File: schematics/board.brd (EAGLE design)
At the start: 49.2 x 38.1 mm, 25 parts, among them IC1 MEGA8-P, M1 PSMN017-30ELL-V, M2 PSMN017-30ELL-V, M3 PSMN017-30ELL-V

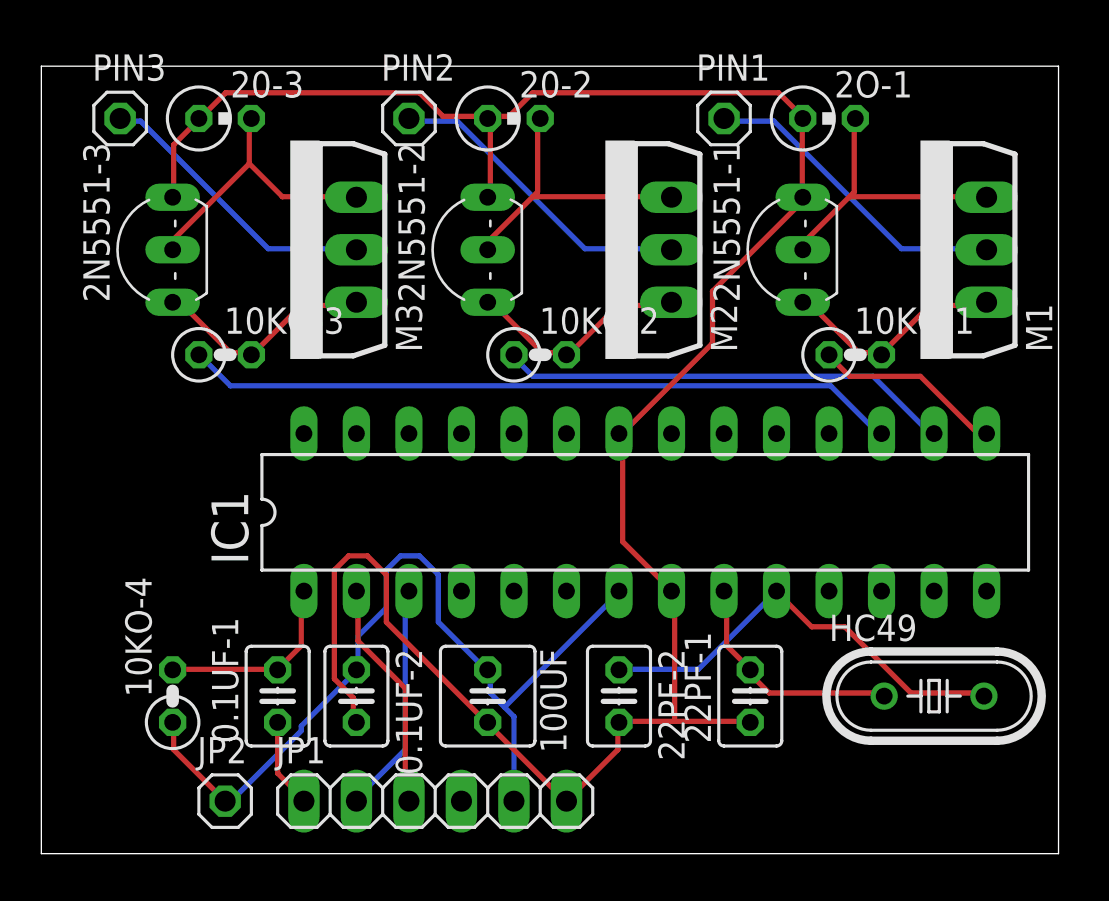
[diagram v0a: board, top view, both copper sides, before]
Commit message: Ajoute alim & logo sur la PCB
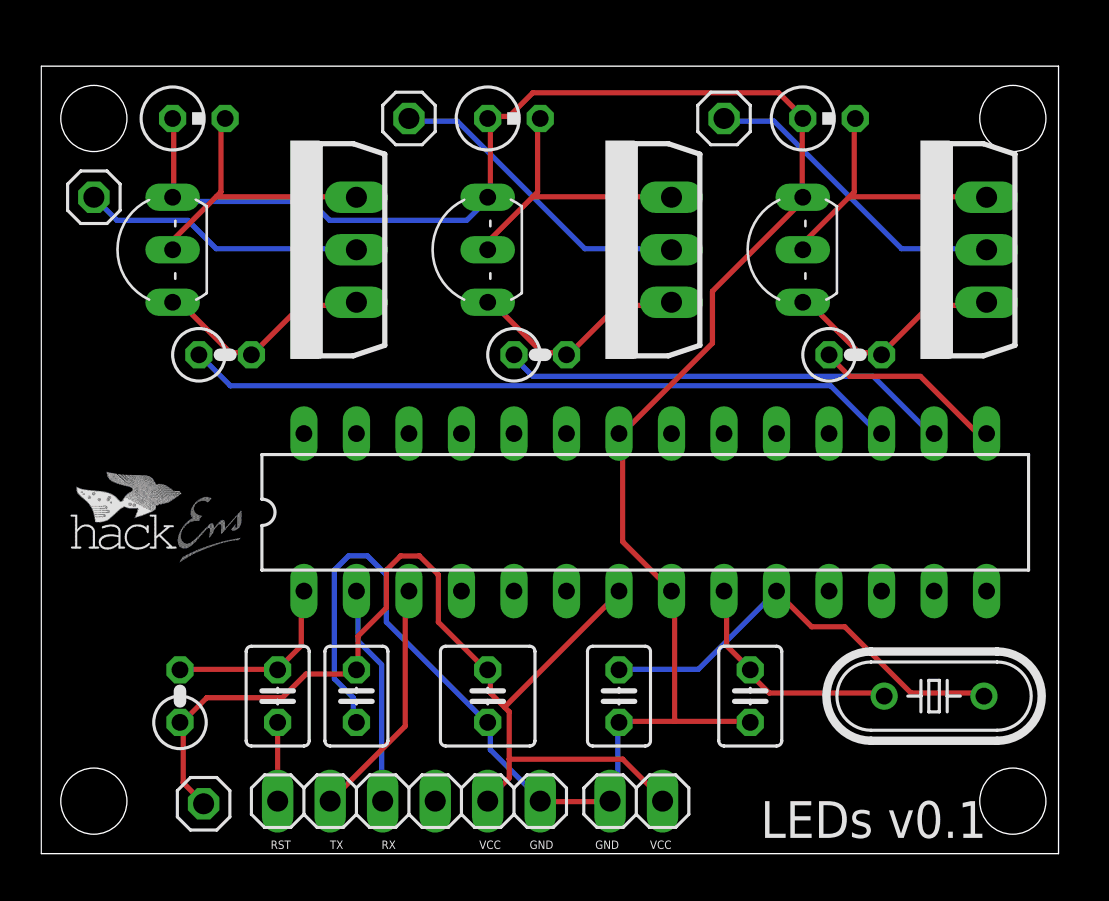
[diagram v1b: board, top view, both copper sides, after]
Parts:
- added POWER: (no value), pinhead:1X02
- added U$1: (no value), hackens:HACKENS-LOGO
- 0.1UF-1, 0.1UF-2: value 0.1μF -> 0.1uF
- 100UF: value 100μF -> 100uF
- 10KO-1, 10KO-2, 10KO-3, 10KO-4: value 10kΩ -> 10k
- 20-2, 20-3, 2O-1: value 2Ω -> 2, 0.6W
- M1, M2, M3: value PSMN017-30ELL-V -> PSMN017-30EL
- moved PIN3 4.02 mm to (2.54, 31.8)
- moved 20-3 1.27 mm to (7.62, 35.6)
- moved JP1 1.27 mm to (17.8, 2.54)
- moved JP2 1.05 mm to (7.85, 2.41)
- moved 10KO-4 0.36 mm to (6.71, 7.62)
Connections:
- net GND: now also POWER.2
- net VCC: now also POWER.1
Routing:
- net VCC: track 43.1 -> 51.6 mm
- net GND: track 110.5 -> 113.2 mm
- net N$9: track 11.2 -> 11.8 mm
- net N$12: track 11.2 -> 10.7 mm
- net N$3: track 4.32 -> 3.81 mm
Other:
- board text added: "GND"
- board text added: "LEDs v0.1"
- board text added: "RST"
- board text added: "RX"
- board text added: "TX"
- board text added: "VCC"

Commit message: Bigger logo
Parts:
- moved U$1 7.73 mm to (0.00, 21.6), turned to 270 degrees
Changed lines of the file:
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@@
 <attribute name="VALUE" x="31.3182" y="5.715" size="1.27" layer="27" rot="R180"/>
 </element>
-<element name="U$1" library="hackens" package="HACKENS-LOGO" value="" x="1.27" y="13.97"/>
+<element name="U$1" library="hackens" package="HACKENS-LOGO" value="" x="0" y="21.59" rot="R270"/>
 </elements>
 <signals>

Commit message: Ajout pins upload
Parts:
- added JP3: (no value), pinhead:1X02
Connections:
- new net N$19: IC1.28, JP3.1
- net GND: now also JP3.2
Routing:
- net GND: track 113.2 -> 121.3 mm
- net N$19: track 0.00 -> 6.69 mm
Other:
- board text added: "upload"
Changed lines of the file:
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@@
 <hole x="2.54" y="2.54" drill="3.2"/>
 <hole x="2.54" y="35.56" drill="3.2"/>
+<text x="5.08" y="11.43" size="1.016" layer="21">upload</text>
 </plain>
 <attributes>
@@
 </element>
 <element name="U$1" library="hackens" package="HACKENS-LOGO" value="" x="0" y="21.59" rot="R270"/>
+<element name="JP3" library="pinhead" package="1X02" value="" x="7.62" y="15.24" smashed="yes" rot="R270">
+<attribute name="VALUE" x="4.445" y="17.78" size="1.27" layer="27" rot="R270"/>
+</element>
 </elements>
 <signals>
@@
 <contactref element="22PF-1" pad="1"/>
 <contactref element="POWER" pad="2"/>
+<contactref element="JP3" pad="2"/>
 <wire x1="6.4008" y1="35.433" x2="6.4008" y2="31.7754" width="0.254" layer="1"/>
 <wire x1="6.4008" y1="31.7754" x2="6.35" y2="31.75" width="0.254" layer="1"/>
@@
 <wire x1="6.4008" y1="31.5468" x2="6.35" y2="31.75" width="0.254" layer="16"/>
 <wire x1="21.4884" y1="31.5468" x2="21.59" y2="31.75" width="0.254" layer="16"/>
-<wire x1="15.0876" y1="7.5438" x2="15.0876" y2="6.4008" width="0.254" layer="16"/>
-<wire x1="14.1732" y1="8.4582" x2="15.0876" y2="7.5438" width="0.254" layer="16"/>
-<wire x1="14.1732" y1="13.716" x2="14.1732" y2="8.4582" width="0.254" layer="16"/>
-<wire x1="14.859" y1="14.4018" x2="14.1732" y2="13.716" width="0.254" layer="16"/>
-<wire x1="15.7734" y1="14.4018" x2="14.859" y2="14.4018" width="0.254" layer="16"/>
-<wire x1="16.6878" y1="13.4874" x2="15.7734" y2="14.4018" width="0.254" layer="16"/>
-<wire x1="16.6878" y1="11.2014" x2="16.6878" y2="13.4874" width="0.254" layer="16"/>
-<wire x1="21.4884" y1="6.4008" x2="16.6878" y2="11.2014" width="0.254" layer="16"/>
+<wire x1="15.0876" y1="6.858" x2="15.0876" y2="6.4008" width="0.254" layer="16"/>
+<wire x1="7.7724" y1="14.1732" x2="12.1158" y2="9.8298" width="0.254" layer="16"/>
+<wire x1="12.1158" y1="9.8298" x2="15.0876" y2="6.858" width="0.254" layer="16"/>
 <wire x1="15.0876" y1="6.4008" x2="15.24" y2="6.35" width="0.254" layer="16"/>
-<wire x1="21.4884" y1="6.4008" x2="21.59" y2="6.35" width="0.254" layer="16"/>
+<wire x1="7.7724" y1="14.1732" x2="7.62" y2="13.97" width="0.254" layer="16"/>
+<wire x1="21.717" y1="5.0292" x2="21.717" y2="6.1722" width="0.254" layer="16"/>
+<wire x1="24.003" y1="2.7432" x2="21.717" y2="5.0292" width="0.254" layer="16"/>
+<wire x1="21.717" y1="6.1722" x2="21.59" y2="6.35" width="0.254" layer="16"/>
+<wire x1="24.003" y1="2.7432" x2="24.13" y2="2.54" width="0.254" layer="16"/>
 <wire x1="36.8046" y1="35.433" x2="36.8046" y2="31.7754" width="0.254" layer="1"/>
 <wire x1="36.8046" y1="31.7754" x2="36.83" y2="31.75" width="0.254" layer="1"/>
@@
 <wire x1="28.1178" y1="20.1168" x2="27.94" y2="20.32" width="0.254" layer="1"/>
 <wire x1="30.4038" y1="12.8016" x2="30.48" y2="12.7" width="0.254" layer="1"/>
-<wire x1="27.432" y1="2.5146" x2="24.2316" y2="2.5146" width="0.254" layer="1"/>
-<wire x1="24.2316" y1="2.5146" x2="24.13" y2="2.54" width="0.254" layer="1"/>
-<wire x1="27.432" y1="2.5146" x2="27.5082" y2="2.54" width="0.254" layer="1"/>
 <wire x1="32.4612" y1="27.2034" x2="36.8046" y2="31.5468" width="0.254" layer="1"/>
 <wire x1="32.4612" y1="24.6888" x2="32.4612" y2="27.2034" width="0.254" layer="1"/>
@@
 <wire x1="36.8046" y1="31.5468" x2="36.83" y2="31.75" width="0.254" layer="1"/>
 <wire x1="28.1178" y1="20.3454" x2="27.94" y2="20.32" width="0.254" layer="1"/>
-<wire x1="21.717" y1="5.0292" x2="21.717" y2="6.1722" width="0.254" layer="16"/>
-<wire x1="24.003" y1="2.7432" x2="21.717" y2="5.0292" width="0.254" layer="16"/>
-<wire x1="21.717" y1="6.1722" x2="21.59" y2="6.35" width="0.254" layer="16"/>
-<wire x1="24.003" y1="2.7432" x2="24.13" y2="2.54" width="0.254" layer="16"/>
+<wire x1="27.432" y1="2.5146" x2="24.2316" y2="2.5146" width="0.254" layer="1"/>
+<wire x1="24.2316" y1="2.5146" x2="24.13" y2="2.54" width="0.254" layer="1"/>
+<wire x1="27.432" y1="2.5146" x2="27.5082" y2="2.54" width="0.254" layer="1"/>
+<wire x1="14.1732" y1="11.8872" x2="12.1158" y2="9.8298" width="0.254" layer="16"/>
+<wire x1="14.1732" y1="13.716" x2="14.1732" y2="11.8872" width="0.254" layer="16"/>
+<wire x1="14.859" y1="14.4018" x2="14.1732" y2="13.716" width="0.254" layer="16"/>
+<wire x1="15.7734" y1="14.4018" x2="14.859" y2="14.4018" width="0.254" layer="16"/>
+<wire x1="16.6878" y1="13.4874" x2="15.7734" y2="14.4018" width="0.254" layer="16"/>
+<wire x1="16.6878" y1="11.2014" x2="16.6878" y2="13.4874" width="0.254" layer="16"/>
+<wire x1="21.4884" y1="6.4008" x2="16.6878" y2="11.2014" width="0.254" layer="16"/>
+<wire x1="21.4884" y1="6.4008" x2="21.59" y2="6.35" width="0.254" layer="16"/>
 <wire x1="22.6314" y1="35.6616" x2="21.717" y2="35.6616" width="0.254" layer="1"/>
 <wire x1="23.7744" y1="36.8046" x2="22.6314" y2="35.6616" width="0.254" layer="1"/>
@@
 <contactref element="2N5551-3" pad="C"/>
 <contactref element="M3" pad="1"/>
-<wire x1="9.144" y1="24.2316" x2="10.0584" y2="24.2316" width="0.254" layer="1"/>
-<wire x1="6.858" y1="26.5176" x2="9.144" y2="24.2316" width="0.254" layer="1"/>
-<wire x1="6.4008" y1="26.5176" x2="6.858" y2="26.5176" width="0.254" layer="1"/>
-<wire x1="10.0584" y1="24.2316" x2="10.16" y2="24.13" width="0.254" layer="1"/>
-<wire x1="6.4008" y1="26.5176" x2="6.35" y2="26.67" width="0.254" layer="1"/>
+<wire x1="9.144" y1="24.2316" x2="10.0584" y2="24.2316" width="0.254" layer="16"/>
+<wire x1="6.858" y1="26.5176" x2="9.144" y2="24.2316" width="0.254" layer="16"/>
+<wire x1="6.4008" y1="26.5176" x2="6.858" y2="26.5176" width="0.254" layer="16"/>
+<wire x1="10.0584" y1="24.2316" x2="10.16" y2="24.13" width="0.254" layer="16"/>
+<wire x1="6.4008" y1="26.5176" x2="6.35" y2="26.67" width="0.254" layer="16"/>
 <wire x1="12.573" y1="26.5176" x2="15.0876" y2="26.5176" width="0.254" layer="1"/>
 <wire x1="10.287" y1="24.2316" x2="12.573" y2="26.5176" width="0.254" layer="1"/>
@@
 <wire x1="33.147" y1="35.433" x2="33.02" y2="35.56" width="0.254" layer="16"/>
 </signal>
+<signal name="N$19">
+<contactref element="IC1" pad="28"/>
+<contactref element="JP3" pad="1"/>
+<wire x1="11.2014" y1="20.1168" x2="12.573" y2="20.1168" width="0.254" layer="1"/>
+<wire x1="7.7724" y1="16.6878" x2="11.2014" y2="20.1168" width="0.254" layer="1"/>
+<wire x1="12.573" y1="20.1168" x2="12.7" y2="20.32" width="0.254" layer="1"/>
+<wire x1="7.7724" y1="16.6878" x2="7.62" y2="16.51" width="0.254" layer="1"/>
+</signal>
 </signals>

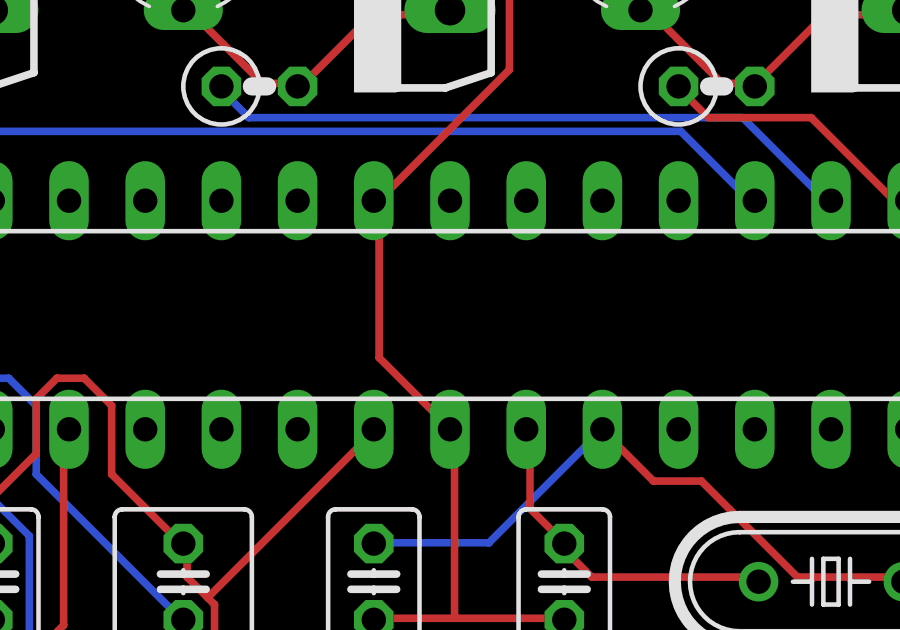
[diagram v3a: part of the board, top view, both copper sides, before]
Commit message: Connecte AVCC et VCC
D'après la datasheet atmel
(http://www.farnell.com/datasheets/1698185.pdf )
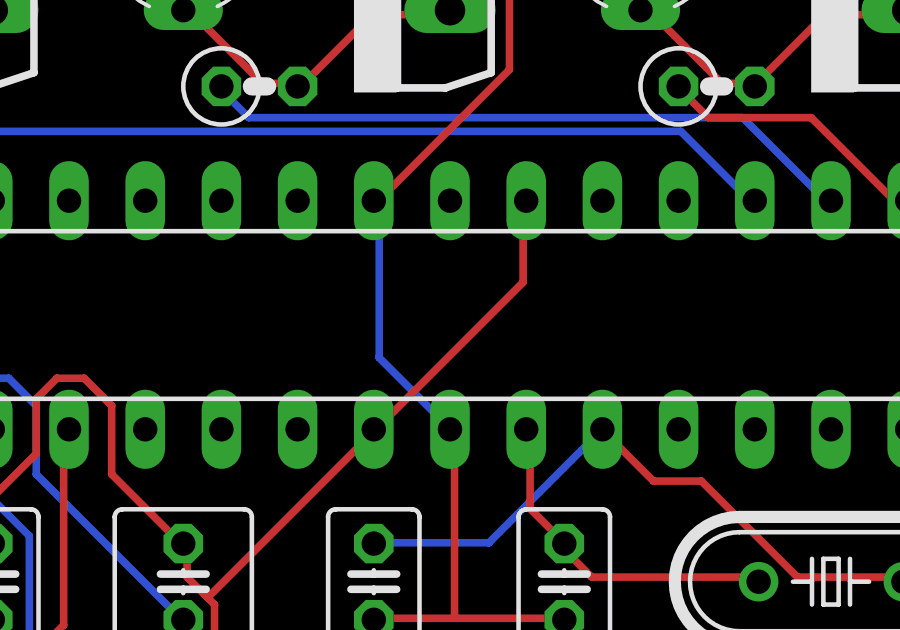
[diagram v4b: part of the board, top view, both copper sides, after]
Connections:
- removed net AVCC: IC1.20
- net VCC: now also IC1.20
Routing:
- net VCC: track 51.6 -> 61.4 mm
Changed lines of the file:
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@@
 </elements>
 <signals>
-<signal name="AVCC">
-<contactref element="IC1" pad="20"/>
-</signal>
 <signal name="GND">
 <contactref element="IC1" pad="22"/>
@@
 <wire x1="30.6324" y1="6.4008" x2="30.6324" y2="12.573" width="0.254" layer="1"/>
 <wire x1="30.6324" y1="12.573" x2="30.48" y2="12.7" width="0.254" layer="1"/>
-<wire x1="28.1178" y1="15.0876" x2="28.1178" y2="20.1168" width="0.254" layer="1"/>
-<wire x1="30.4038" y1="12.8016" x2="28.1178" y2="15.0876" width="0.254" layer="1"/>
-<wire x1="28.1178" y1="20.1168" x2="27.94" y2="20.32" width="0.254" layer="1"/>
-<wire x1="30.4038" y1="12.8016" x2="30.48" y2="12.7" width="0.254" layer="1"/>
+<wire x1="28.1178" y1="15.0876" x2="28.1178" y2="20.1168" width="0.254" layer="16"/>
+<wire x1="30.4038" y1="12.8016" x2="28.1178" y2="15.0876" width="0.254" layer="16"/>
+<wire x1="28.1178" y1="20.1168" x2="27.94" y2="20.32" width="0.254" layer="16"/>
+<wire x1="30.4038" y1="12.8016" x2="30.48" y2="12.7" width="0.254" layer="16"/>
 <wire x1="32.4612" y1="27.2034" x2="36.8046" y2="31.5468" width="0.254" layer="1"/>
 <wire x1="32.4612" y1="24.6888" x2="32.4612" y2="27.2034" width="0.254" layer="1"/>
@@
 <contactref element="JP2" pad="1"/>
 <contactref element="POWER" pad="1"/>
+<contactref element="IC1" pad="20"/>
 <wire x1="6.858" y1="3.429" x2="6.858" y2="6.1722" width="0.254" layer="1"/>
 <wire x1="7.7724" y1="2.5146" x2="6.858" y2="3.429" width="0.254" layer="1"/>
@@
 <wire x1="22.4028" y1="7.0866" x2="27.8892" y2="12.573" width="0.254" layer="1"/>
 <wire x1="27.8892" y1="12.573" x2="27.94" y2="12.7" width="0.254" layer="1"/>
+<wire x1="32.9184" y1="17.6022" x2="32.9184" y2="20.1168" width="0.254" layer="1"/>
+<wire x1="28.1178" y1="12.8016" x2="32.9184" y2="17.6022" width="0.254" layer="1"/>
+<wire x1="32.9184" y1="20.1168" x2="33.02" y2="20.32" width="0.254" layer="1"/>
+<wire x1="28.1178" y1="12.8016" x2="27.94" y2="12.7" width="0.254" layer="1"/>
 <wire x1="28.1178" y1="4.572" x2="29.9466" y2="2.7432" width="0.254" layer="1"/>
 <wire x1="22.6314" y1="4.572" x2="28.1178" y2="4.572" width="0.254" layer="1"/>
